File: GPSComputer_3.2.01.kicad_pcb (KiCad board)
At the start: 4 copper layers, 96 x 96 mm, 68 parts, among them J1 GPS_ANT_3, J2 GPS_ANT_0, J3 GPS_ANT_2, J4 2125281600, J5 Conn_02x08_Odd_Even, J6 Conn_02x08_Odd_Even, U1 NEO-6M-GPS, U2 24AA32A-I_ST, U3 NEO-6M-GPS, U4 NEO-6M-GPS, U5 24AA32A-I_ST, U7 STM32F405RGTx, Y1 8MHz

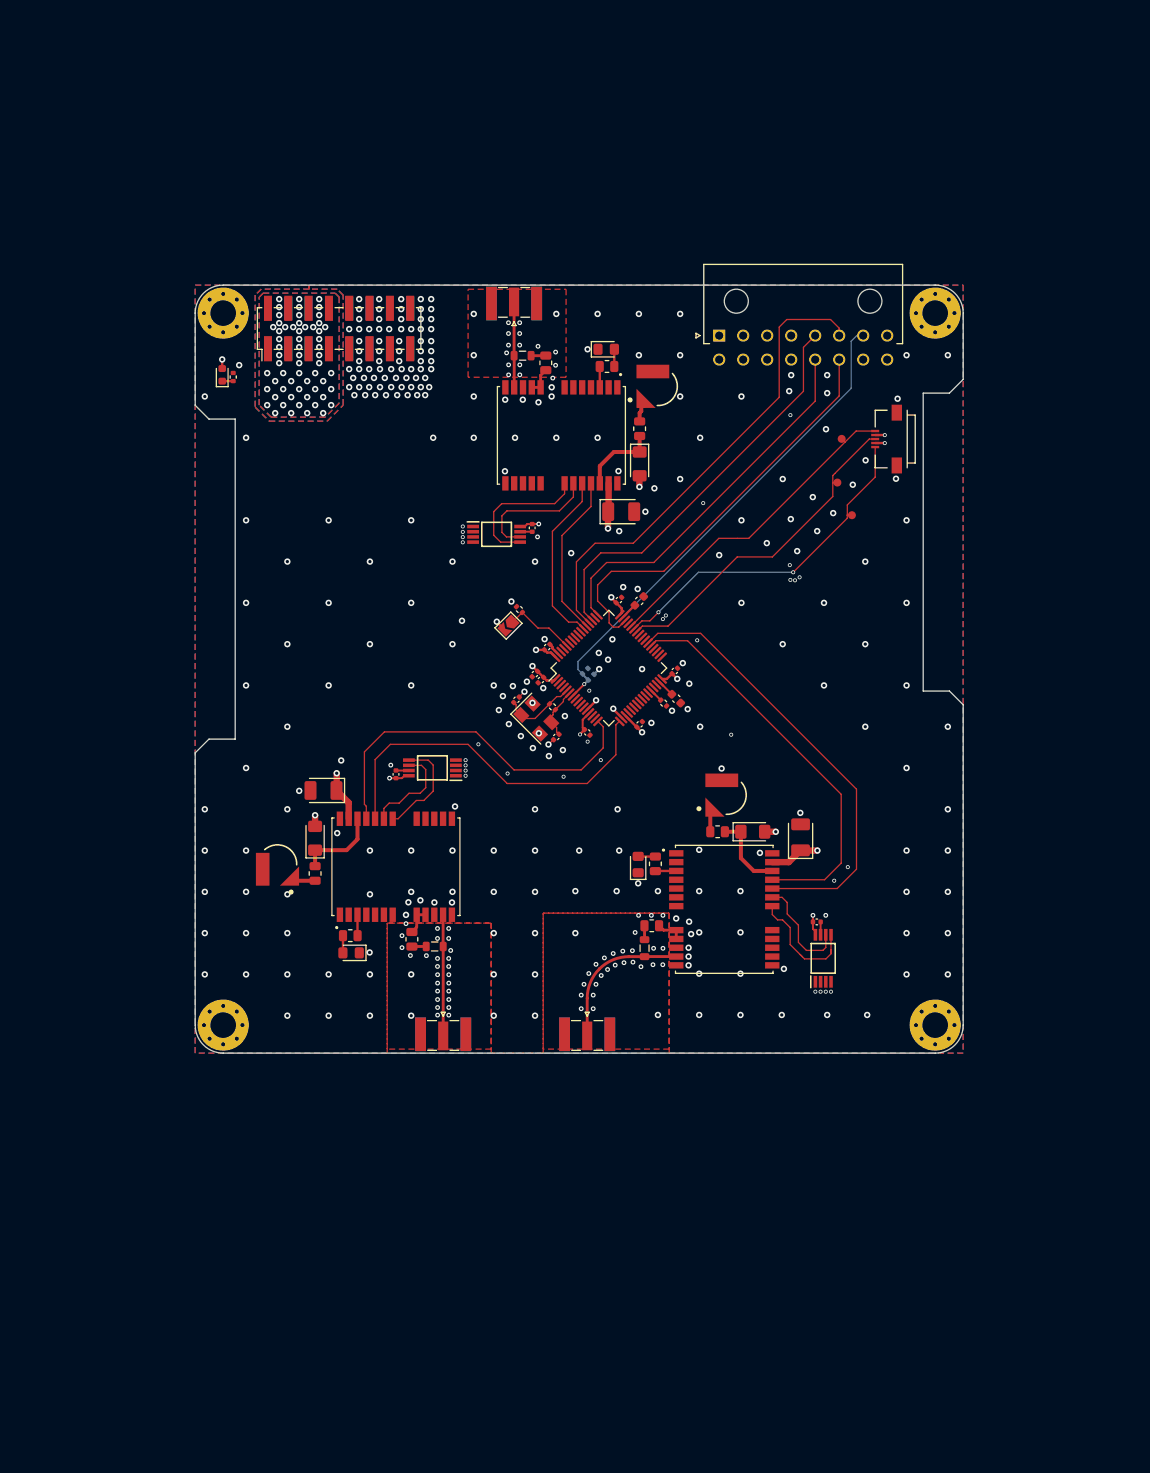
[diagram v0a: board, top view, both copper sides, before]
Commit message: Adding M10
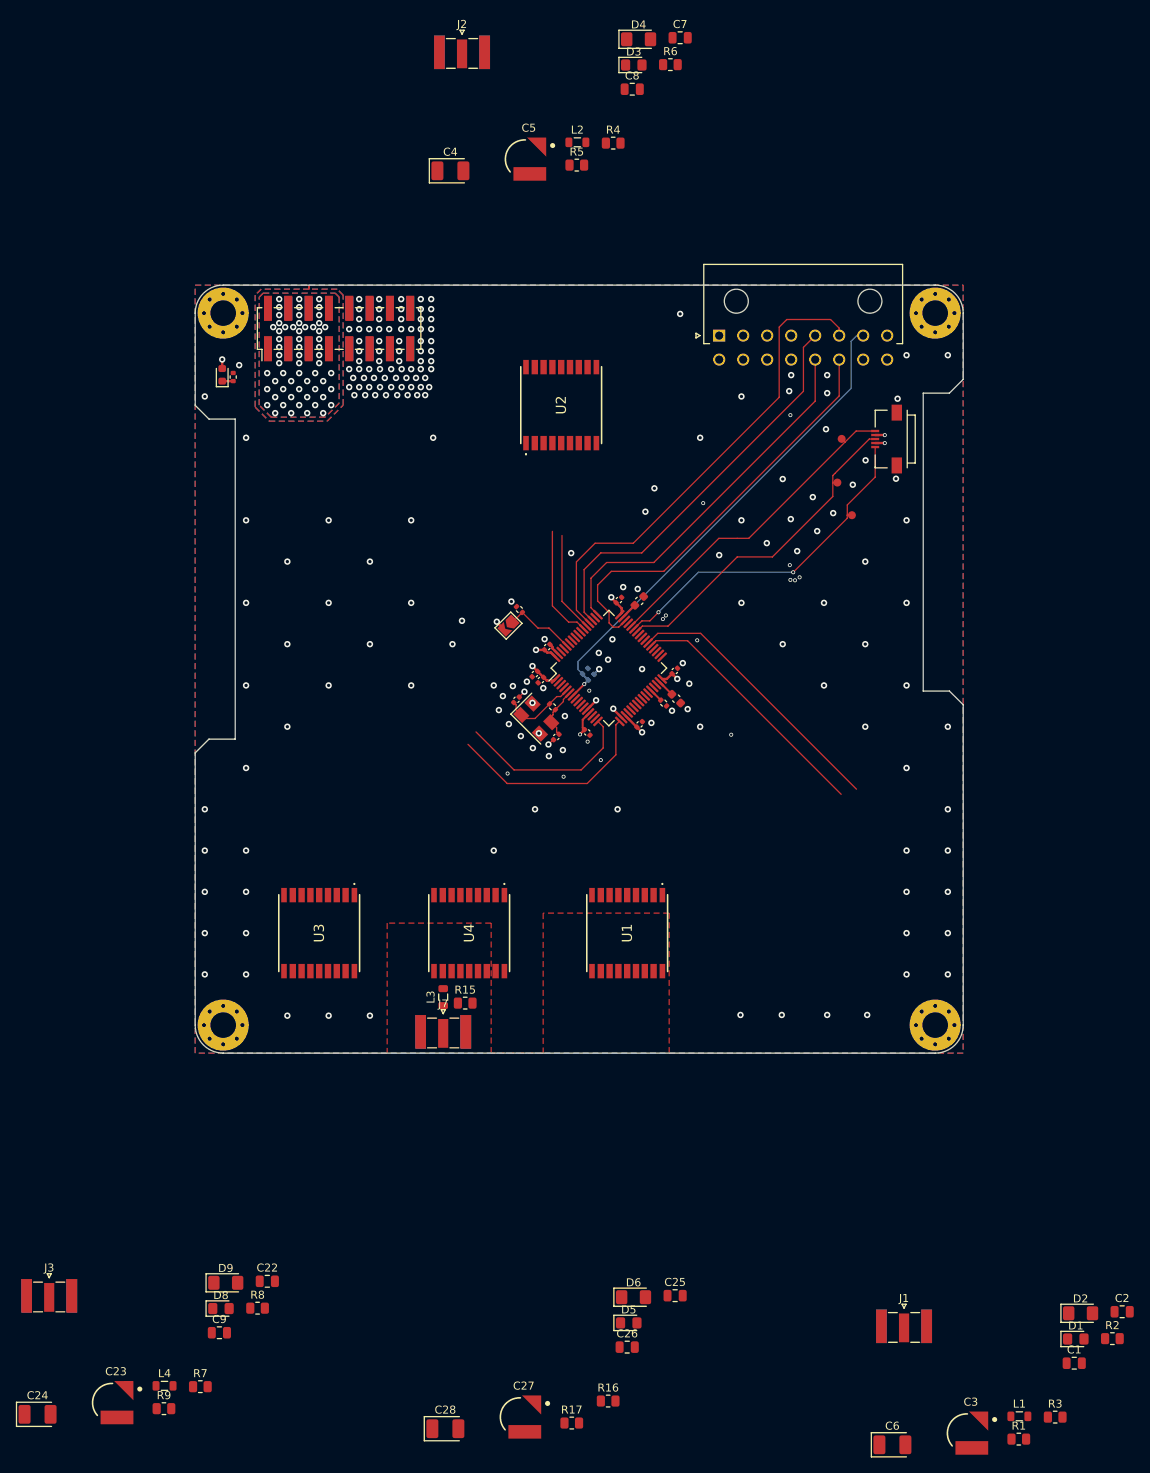
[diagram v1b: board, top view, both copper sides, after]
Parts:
- removed EEP1, U5: 24AA32A-I_ST, 24AA32A-I_ST:SOP65P640X120-8N
- added C22: 1.0 uF, Capacitor_SMD:C_0805_2012Metric, F.Cu at (111.0, 172.5)
- added C23: XH414H-IV01E, XH414H:CAP_XH414H-IV01E, F.Cu at (91.6, 187.7)
- added C24: 1uF, Capacitor_Tantalum_SMD:CP_EIA-3528-21_Kemet-B_Pad1.50x2.35mm_HandSolder, F.Cu at (82.3, 189.2)
- added C25: 10nF, Capacitor_SMD:C_0805_2012Metric, F.Cu at (162.0, 174.3)
- added C26: 1.0 uF, Capacitor_SMD:C_0805_2012Metric, F.Cu at (156.0, 180.8)
- added C27: XH414H-IV01E, XH414H:CAP_XH414H-IV01E, F.Cu at (142.6, 189.5)
- added C28: 1uF, Capacitor_Tantalum_SMD:CP_EIA-3528-21_Kemet-B_Pad1.50x2.35mm_HandSolder, F.Cu at (133.3, 190.9)
- added D8: LED, LED_SMD:LED_0805_2012Metric_Pad1.15x1.40mm_HandSolder, F.Cu at (105.2, 175.9)
- added D9: D, Diode_SMD:D_1206_3216Metric_Pad1.42x1.75mm_HandSolder, F.Cu at (105.8, 172.7)
- added J7: GPS_ANT_0, Connector_Coaxial:SMA_Samtec_SMA-J-P-X-ST-EM1_EdgeMount, F.Cu at (133.0, 141.3)
- added L4: 27nH, Inductor_SMD:L_0805_2012Metric, F.Cu at (98.2, 185.6)
- added R15: 10R, Resistor_SMD:R_0805_2012Metric, F.Cu at (135.8, 137.8)
- added R16: 1K, Resistor_SMD:R_0805_2012Metric, F.Cu at (153.6, 187.5)
- added R17: 1K, Resistor_SMD:R_0805_2012Metric, F.Cu at (149.1, 190.2)
- C1, C7: value 1uF -> 10nF; footprint Capacitor_Tantalum_SMD:CP_EIA-3528-21_Kemet-B_Pad1.50x2.35mm_HandSolder -> Capacitor_SMD:C_0805_2012Metric
- C2, C8: value XH414H-IV01E -> 1.0 uF; footprint XH414H:CAP_XH414H-IV01E -> Capacitor_SMD:C_0805_2012Metric
- C3: value 100n -> XH414H-IV01E; footprint Capacitor_SMD:C_0402_1005Metric -> XH414H:CAP_XH414H-IV01E
- C6: value 100n -> 1uF; footprint Capacitor_SMD:C_0402_1005Metric -> Capacitor_Tantalum_SMD:CP_EIA-3528-21_Kemet-B_Pad1.50x2.35mm_HandSolder
- C9: value 100n -> 10nF; footprint Capacitor_SMD:C_0402_1005Metric -> Capacitor_SMD:C_0805_2012Metric
- J1: value GPS_ANT_3 -> GPS_ANT_0
- J3: value GPS_ANT_2 -> GPS_ANT_0
- L1, L2, L3: value 27uH -> 27nH
- R1, R4, R7: value 22R -> 10R
- U1, U3, U4: value NEO-6M-GPS -> MAX-M10S-00B; footprint NEO 6M:XCVR_NEO-6M-GPS -> MAX-M10S-00B:MAXM10S00B
- U2: value 24AA32A-I_ST -> MAX-M10S-00B; footprint 24AA32A-I_ST:SOP65P640X120-8N -> MAX-M10S-00B:MAXM10S00B
- moved C6 123.1 mm to (189.2, 193.0), turned to 0 degrees
- moved C8 106.5 mm to (156.6, 23.5), turned to 0 degrees
- moved C7 104.1 mm to (162.6, 17.1), turned to 0 degrees
- moved R3 84.5 mm to (209.5, 189.5)
- moved R2 82.4 mm to (216.7, 179.7), turned to 0 degrees
- moved C2 81.3 mm to (217.9, 176.3), turned to 0 degrees
- moved D1 80.7 mm to (212.1, 179.7), turned to 0 degrees
- moved R1 78.9 mm to (204.9, 192.2)
- moved U2 76.5 mm to (147.8, 63.0), turned to -90 degrees
- moved L1 75.0 mm to (205.0, 189.4), turned to 0 degrees
- moved C1 74.1 mm to (211.9, 182.8), turned to 0 degrees
- moved C9 73.2 mm to (105.0, 179.0), turned to 0 degrees
- moved D2 72.8 mm to (212.7, 176.5)
- moved D6 69.8 mm to (156.8, 174.5), turned to 0 degrees
- moved R9 69.5 mm to (98.1, 188.4), turned to 0 degrees
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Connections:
- C1 pad 1: +3.3V -> Net-(C1-Pad1)
- C2 pad 1: Net-(C2-Pad1) -> GPS2_V_BCKP
- C3 pad 1: +3.3V -> GPS2_V_BCKP
- C5 pad 1: Net-(C5-Pad1) -> GPS0_V_BCKP
- C7 pad 1: +3.3V -> Net-(R4-Pad1)
- C8 pad 1: Net-(C8-Pad1) -> GPS0_V_BCKP
- C9 pad 1: +3.3V -> Net-(C9-Pad1)
- D2 pad 1: GPS3_V_BCKP -> Net-(D2-Pad1)
- D4 pad 1: GPS0_V_BCKP -> Net-(D4-Pad1)
- D6 pad 1: GPS2_V_BCKP -> Net-(D6-Pad1)
- L1 pad 1: Net-(L1-Pad1) -> Net-(C1-Pad1)
- L2 pad 1: Net-(L2-Pad1) -> Net-(R4-Pad1)
- L3 pad 1: Net-(L3-Pad1) -> Net-(C25-Pad1)
- L3 pad 2: Net-(J3-Pad1) -> Net-(J7-Pad1)
- R1 pad 1: Net-(L1-Pad1) -> Net-(C1-Pad1)
- R1 pad 2: GPS3_VCC_RF -> Net-(R1-Pad2)
- R2 pad 2: GPS3_TIMEPULSE -> GPS2_TIMEPULSE
- R3 pad 1: Net-(C2-Pad1) -> GPS2_V_BCKP
- R3 pad 2: GPS3_V_BCKP -> Net-(D2-Pad1)
- R4 pad 1: Net-(L2-Pad1) -> Net-(R4-Pad1)
- R4 pad 2: GPS0_VCC_RF -> Net-(R4-Pad2)
- R6 pad 1: Net-(C5-Pad1) -> GPS0_V_BCKP
- R6 pad 2: GPS0_V_BCKP -> Net-(D4-Pad1)
- R7 pad 1: Net-(L3-Pad1) -> Net-(C9-Pad1)
- R7 pad 2: GPS2_VCC_RF -> Net-(R7-Pad2)
- R8 pad 1: Net-(D5-Pad2) -> Net-(D8-Pad2)
- R8 pad 2: GPS2_TIMEPULSE -> GPS3_TIMEPULSE
- R9 pad 1: Net-(C8-Pad1) -> GPS3_V_BCKP
- R9 pad 2: GPS2_V_BCKP -> Net-(D9-Pad1)
- U1 pad 1: (no net) -> GND
- U1 pad 13: GND -> unconnected-(U1-Pad13)
- U1 pad 14: unconnected-(U1-Pad14) -> Net-(R1-Pad2)
- U1 pad 18: GPS3_I2C_SDA -> unconnected-(U1-Pad18)
- U1 pad 2: unconnected-(U1-Pad2) -> GPS2_USART6_RX
- U1 pad 3: GPS3_TIMEPULSE -> GPS2_USART6_TX
- U1 pad 4: unconnected-(U1-Pad4) -> GPS2_TIMEPULSE
- U1 pad 6: unconnected-(U1-Pad6) -> GPS2_V_BCKP
- U1 pad 8: GPS3_VCC_RF -> +3.3V
- U1 pad 9: GPS3_VCC_RF -> GPS2_RST
- U2 pad 2: GND -> GPS0_UART5_RX
- U2 pad 3: GND -> GPS0_UART5_TX
- U2 pad 4: GND -> GPS0_TIMEPULSE
- U2 pad 5: GPS3_I2C_SDA -> unconnected-(U2-Pad5)
- U2 pad 6: GPS3_I2C_SCL -> GPS0_V_BCKP
- U3 pad 1: (no net) -> GND
- U3 pad 11: Net-(J2-Pad1) -> Net-(J3-Pad1)
- U3 pad 13: GND -> unconnected-(U3-Pad13)
- U3 pad 14: unconnected-(U3-Pad14) -> Net-(R7-Pad2)
- U3 pad 18: GPS0_I2C_SDA -> unconnected-(U3-Pad18)
- U3 pad 3: GPS0_TIMEPULSE -> unconnected-(U3-Pad3)
- U3 pad 4: unconnected-(U3-Pad4) -> GPS3_TIMEPULSE
- U3 pad 6: unconnected-(U3-Pad6) -> GPS3_V_BCKP
- U3 pad 8: GPS0_VCC_RF -> +3.3V
- U3 pad 9: GPS0_VCC_RF -> GPS3_RST
- U4 pad 1: (no net) -> GND
- U4 pad 11: Net-(J3-Pad1) -> Net-(J7-Pad1)
- U4 pad 13: GND -> unconnected-(U4-Pad13)
- U4 pad 14: unconnected-(U4-Pad14) -> Net-(R15-Pad2)
- U4 pad 18: GPS2_I2C_SDA -> unconnected-(U4-Pad18)
- U4 pad 2: unconnected-(U4-Pad2) -> GPS1_USART2_RX
- U4 pad 3: GPS2_TIMEPULSE -> GPS1_USART2_TX
- U4 pad 4: unconnected-(U4-Pad4) -> GPS1_TIMEPULSE
- U4 pad 6: unconnected-(U4-Pad6) -> GPS1_V_BCKP
- U4 pad 8: GPS2_VCC_RF -> +3.3V
- U4 pad 9: GPS2_VCC_RF -> GPS1_RST
- U7 pad 16: GPS2_USART2_TX -> GPS1_USART2_TX
- U7 pad 17: GPS2_USART2_RX -> GPS1_USART2_RX
- U7 pad 37: GPS3_USART6_TX -> GPS2_USART6_TX
- U7 pad 38: GPS3_USART6_RX -> GPS2_USART6_RX
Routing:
- net GPS3_USART6_RX: track 56.2 -> 0.00 mm
- net GPS3_USART6_TX: track 50.1 -> 0.00 mm
- net GPS2_USART2_RX: track 46.2 -> 0.00 mm
- net GPS2_USART2_TX: track 46.0 -> 0.00 mm
- net GPS2_USART6_RX: track 0.00 -> 34.6 mm
- net GPS2_USART6_TX: track 0.00 -> 32.0 mm
- net +3.3V: track 51.6 -> 21.6 mm, vias 78 -> 69
- net GPS1_USART2_RX: track 0.00 -> 26.4 mm
- net GPS1_USART2_TX: track 0.00 -> 22.6 mm
- net Net-(J1-Pad1): track 18.8 -> 0.00 mm
- net GPS0_I2C_SDA: track 17.7 -> 0.00 mm
- net GPS0_I2C_SCL: track 16.2 -> 0.00 mm
- net GPS3_I2C_SDA: track 15.3 -> 0.00 mm
- net Net-(J3-Pad1): track 15.2 -> 0.00 mm
- net GPS3_I2C_SCL: track 13.3 -> 0.00 mm
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
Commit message: Finished M10
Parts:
- C1, C25, C7, C9: footprint Capacitor_SMD:C_0805_2012Metric -> Capacitor_SMD:C_0402_1005Metric
- L1, L2, L3, L4: footprint Inductor_SMD:L_0805_2012Metric -> Inductor_SMD:L_0402_1005Metric
- R1, R15, R4, R7: footprint Resistor_SMD:R_0805_2012Metric -> Resistor_SMD:R_0402_1005Metric
- moved R3 95.7 mm to (148.1, 116.2), turned to 180 degrees
- moved C3 92.3 mm to (151.1, 112.2), turned to 180 degrees
- moved D2 92.3 mm to (146.2, 112.5), turned to 90 degrees
- moved C2 90.9 mm to (148.1, 118.0), turned to 180 degrees
- moved R2 88.3 mm to (151.7, 119.9), turned to -90 degrees
- moved D1 86.3 mm to (152.7, 117.2), turned to 180 degrees
- moved C6 81.3 mm to (143.0, 126.0), turned to 90 degrees
- moved C23 78.6 mm to (112.7, 111.9), turned to -90 degrees
- moved C27 78.6 mm to (130.1, 111.9), turned to -90 degrees
- moved R1 77.8 mm to (150.4, 136.8)
- moved L1 77.5 mm to (148.1, 136.8), turned to 180 degrees
- moved R17 76.2 mm to (131.2, 116.2), turned to 180 degrees
- moved C1 76.1 mm to (150.4, 137.9)
- moved R9 74.0 mm to (113.8, 116.2), turned to 180 degrees
- moved R16 70.0 mm to (135.2, 119.9), turned to -90 degrees
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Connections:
- U1 pad 9: GPS2_RST -> GPS2_RESET
- U2 pad 9: GPS0_RST -> GPS0_RESET
- U3 pad 2: unconnected-(U3-Pad2) -> GPS3_USART2_RX
- U3 pad 3: unconnected-(U3-Pad3) -> GPS3_USART2_TX
- U3 pad 9: GPS3_RST -> GPS3_RESET
- U4 pad 2: GPS1_USART2_RX -> GPS1_USART3_RX
- U4 pad 3: GPS1_USART2_TX -> GPS1_USART3_TX
- U4 pad 9: GPS1_RST -> GPS1_RESET
- U7 pad 15: unconnected-(U7-Pad15) -> GPS3_RESET
- U7 pad 16: GPS1_USART2_TX -> GPS3_USART2_TX
- U7 pad 17: GPS1_USART2_RX -> GPS3_USART2_RX
- U7 pad 23: unconnected-(U7-Pad23) -> GPS1_RESET
- U7 pad 29: unconnected-(U7-Pad29) -> GPS1_USART3_TX
- U7 pad 30: unconnected-(U7-Pad30) -> GPS1_USART3_RX
- U7 pad 34: unconnected-(U7-Pad34) -> GPS2_RESET
- U7 pad 55: unconnected-(U7-Pad55) -> GPS0_RESET
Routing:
- net GPS3_RESET: track 0.00 -> 53.6 mm
- net GPS0_RESET: track 0.00 -> 42.0 mm, vias 0 -> 2
- net +3.3V: track 21.6 -> 60.9 mm, vias 69 -> 77
- net GPS1_RESET: track 0.00 -> 38.7 mm
- net GPS3_USART2_TX: track 0.00 -> 32.3 mm
- net GPS2_RESET: track 0.00 -> 32.0 mm
- net GPS3_USART2_RX: track 0.00 -> 31.5 mm
- net GPS1_USART2_RX: track 26.4 -> 0.00 mm
- net GPS1_USART3_TX: track 0.00 -> 25.9 mm
- net GPS1_USART3_RX: track 0.00 -> 25.6 mm
- net GPS1_USART2_TX: track 22.6 -> 0.00 mm
- net FLI_GPS_USART1_TX: track 41.9 -> 56.1 mm
- net FLI_GPS_USART1_RX: track 43.3 -> 56.7 mm
- net FLI_GPS_USART1_CTS: track 41.2 -> 53.7 mm
- net GPS3_V_BCKP: track 0.00 -> 10.9 mm
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
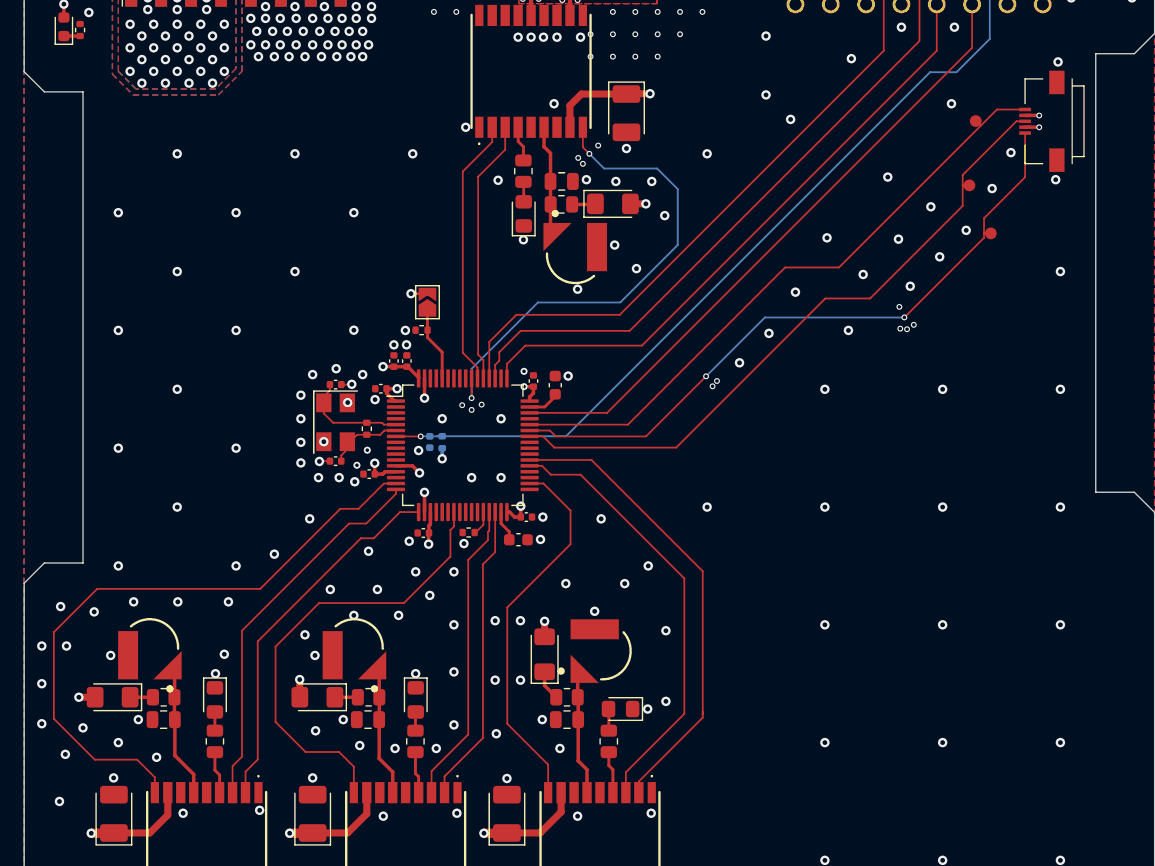
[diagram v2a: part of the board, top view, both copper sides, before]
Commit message: Corrected battery position
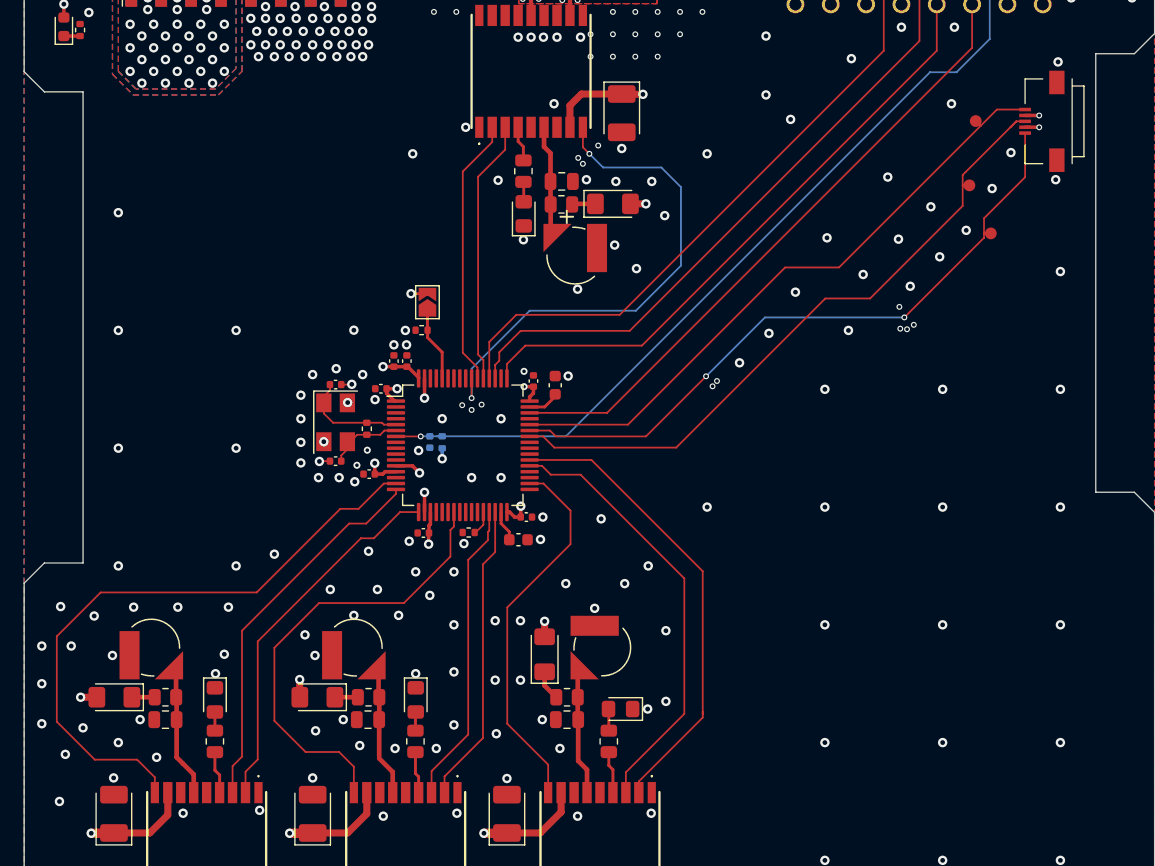
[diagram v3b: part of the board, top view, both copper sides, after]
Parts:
- removed C23, C27, C3, C5: XH414H-IV01E, XH414H:CAP_XH414H-IV01E
- added BT1: ML414H_IV01E, ML414H IV01E:SEIKO_ML414H_IV01E, F.Cu at (151.1, 111.9)
- added BT2: ML414H_IV01E, ML414H IV01E:SEIKO_ML414H_IV01E, F.Cu at (148.8, 78.7)
- added BT3: ML414H_IV01E, ML414H IV01E:SEIKO_ML414H_IV01E, F.Cu at (130.0, 111.9)
- added BT4: ML414H_IV01E, ML414H IV01E:SEIKO_ML414H_IV01E, F.Cu at (112.8, 111.9)
- moved C4 0.40 mm to (152.8, 66.5)
- moved C22 0.15 mm to (114.0, 118.0)
- moved R9 0.15 mm to (114.0, 116.2)
- moved D9 0.15 mm to (109.7, 116.2)
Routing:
- net GPS0_RESET: track 42.0 -> 43.7 mm
- net FLI_GPS_USART1_TX: track 56.1 -> 56.8 mm
- net +3.3V: track 60.9 -> 60.3 mm
- net GPS3_RESET: track 53.6 -> 53.0 mm
- net GND: vias 501 -> 492
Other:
- board text added: "Y = 67.2425"
- board text removed: "Y = 67.24"
